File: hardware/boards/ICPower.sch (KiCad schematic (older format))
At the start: 35 parts, among them U1 ECP5UM5G-381caBGA, U3 CYUSB3014, U4 IS43TR16256B-125KBL, U5 128MiB

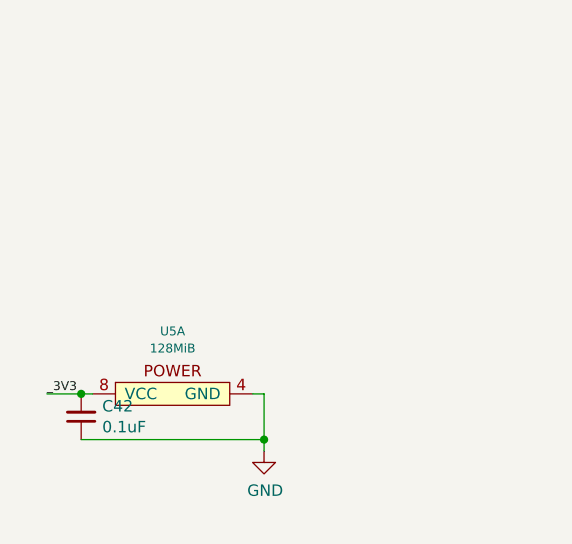
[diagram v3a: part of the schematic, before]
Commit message: Added a secondary SPI flash for the USB PHY Firmware. Yes it's overkill but it'll be fine. I'll use it to like, store configuration data or something
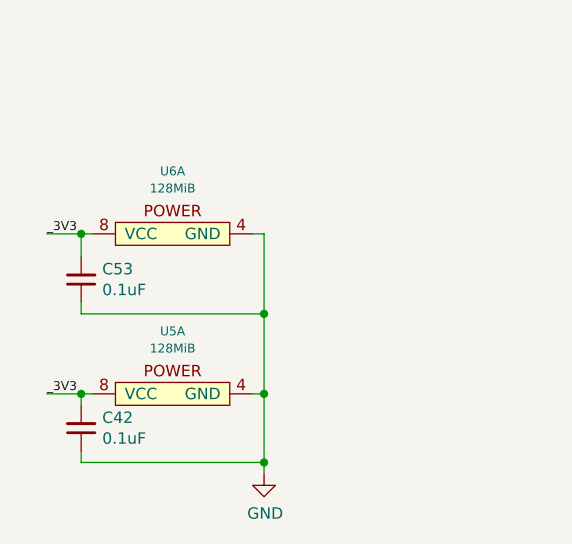
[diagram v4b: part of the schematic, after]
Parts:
- added C53: 0.1uF, Capacitor_SMD:C_0603_1608Metric, symbol Device:C_Small
- added U6: 128MiB, lethalbit-memory:WSON-8-1EP-6.0x8.0mm, symbol lethalbit-memory:W25N01GVZEIG
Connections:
- net 3V3: now also C53.2, U6.8 (VCC)
- net GND: now also C53.1, U6.4 (GND), U6.9 (GND)
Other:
- moved on the sheet: C42
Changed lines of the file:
@@
 	1    0    0    -1
 $EndComp
-Wire Wire Line
-	850  10250 700  10250
 Text Label 700  10250 0    39   ~ 0
 _3V3
@@
 L power:GND #PWR0122
 U 1 1 5F6C47FF
-P 1650 10500
-F 0 "#PWR0122" H 1650 10250 50  0001 C CNN
-F 1 "GND" H 1655 10327 50  0000 C CNN
-F 2 "" H 1650 10500 50  0001 C CNN
-F 3 "" H 1650 10500 50  0001 C CNN
-	1    1650 10500
+P 1650 10600
+F 0 "#PWR0122" H 1650 10350 50  0001 C CNN
+F 1 "GND" H 1655 10427 50  0000 C CNN
+F 2 "" H 1650 10600 50  0001 C CNN
+F 3 "" H 1650 10600 50  0001 C CNN
+	1    1650 10600
 	1    0    0    -1
 $EndComp
 Wire Wire Line
 	1600 10250 1650 10250
-Wire Wire Line
-	1650 10250 1650 10450
 $Comp
 L Device:C_Small C?
 U 1 1 5F7157B7
-P 850 10350
+P 850 10400
 AR Path="/5EDF9F51/5F7157B7" Ref="C?"  Part="1"
 AR Path="/5EF66188/5F7157B7" Ref="C42"  Part="1"
-F 0 "C42" H 758 10304 50  0000 R CNN
-F 1 "0.1uF" H 758 10395 50  0000 R CNN
-F 2 "Capacitor_SMD:C_0603_1608Metric" H 850 10350 50  0001 C CNN
-F 3 "~" H 850 10350 50  0001 C CNN
-F 4 "KEMET" V 850 10350 50  0001 C CNN "MFR"
-F 5 "C0603C104M5RACTU" V 850 10350 50  0001 C CNN "MPN"
-	1    850  10350
+F 0 "C42" H 758 10354 50  0000 R CNN
+F 1 "0.1uF" H 758 10445 50  0000 R CNN
+F 2 "Capacitor_SMD:C_0603_1608Metric" H 850 10400 50  0001 C CNN
+F 3 "~" H 850 10400 50  0001 C CNN
+F 4 "KEMET" V 850 10400 50  0001 C CNN "MFR"
+F 5 "C0603C104M5RACTU" V 850 10400 50  0001 C CNN "MPN"
+	1    850  10400
 	-1   0    0    1
 $EndComp
-Wire Wire Line
-	850  10250 900  10250
-Connection ~ 850  10250
-Wire Wire Line
-	850  10450 1650 10450
-Connection ~ 1650 10450
-Wire Wire Line
-	1650 10450 1650 10500
 Text HLabel 800  1200 0    39   Input ~ 0
 VBUS
@@
 Connection ~ 9500 8350
 Connection ~ 9600 8450
+$Comp
+L lethalbit-memory:W25N01GVZEIG U6
+U 1 1 5FEF8524
+P 1250 9500
+F 0 "U6" H 1250 9724 39  0000 C CNN
+F 1 "128MiB" H 1250 9649 39  0000 C CNN
+F 2 "lethalbit-memory:WSON-8-1EP-6.0x8.0mm" H 1250 9650 39  0001 C CNN
+F 3 "https://www.winbond.com/resource-files/w25n01gv%20revl%20050918%20unsecured.pdf" H 1250 9650 39  0001 C CNN
+F 4 "Winbond" H 1250 9500 50  0001 C CNN "MFR"
+F 5 "W25N01GVZEIG" H 1250 9500 50  0001 C CNN "MPN"
+	1    1250 9500
+	1    0    0    -1
+$EndComp
+Wire Wire Line
+	700  10250 850  10250
+Wire Wire Line
+	850  10250 850  10300
+Connection ~ 850  10250
+Wire Wire Line
+	850  10250 900  10250
+$Comp
+L Device:C_Small C?
+U 1 1 5FF1F758
+P 850 9750
+AR Path="/5EDF9F51/5FF1F758" Ref="C?"  Part="1"
+AR Path="/5EF66188/5FF1F758" Ref="C53"  Part="1"
+F 0 "C53" H 758 9704 50  0000 R CNN
+F 1 "0.1uF" H 758 9795 50  0000 R CNN
+F 2 "Capacitor_SMD:C_0603_1608Metric" H 850 9750 50  0001 C CNN
+F 3 "~" H 850 9750 50  0001 C CNN
+F 4 "KEMET" V 850 9750 50  0001 C CNN "MFR"
+F 5 "C0603C104M5RACTU" V 850 9750 50  0001 C CNN "MPN"
+	1    850  9750
+	-1   0    0    1
+$EndComp
+Wire Wire Line
+	1600 9550 1650 9550
+Wire Wire Line
+	1650 9550 1650 9900
+Connection ~ 1650 10250
+Wire Wire Line
+	900  9550 850  9550
+Wire Wire Line
+	850  9650 850  9550
+Connection ~ 850  9550
+Wire Wire Line
+	850  9550 700  9550
+Wire Wire Line
+	850  9850 850  9900
+Wire Wire Line
+	850  9900 1650 9900
+Connection ~ 1650 9900
+Wire Wire Line
+	1650 9900 1650 10250
+Wire Wire Line
+	1650 10250 1650 10550
+Wire Wire Line
+	850  10500 850  10550
+Wire Wire Line
+	850  10550 1650 10550
+Connection ~ 1650 10550
+Wire Wire Line
+	1650 10550 1650 10600
+Text Label 700  9550 0    39   ~ 0
+_3V3
 $EndSCHEMATC

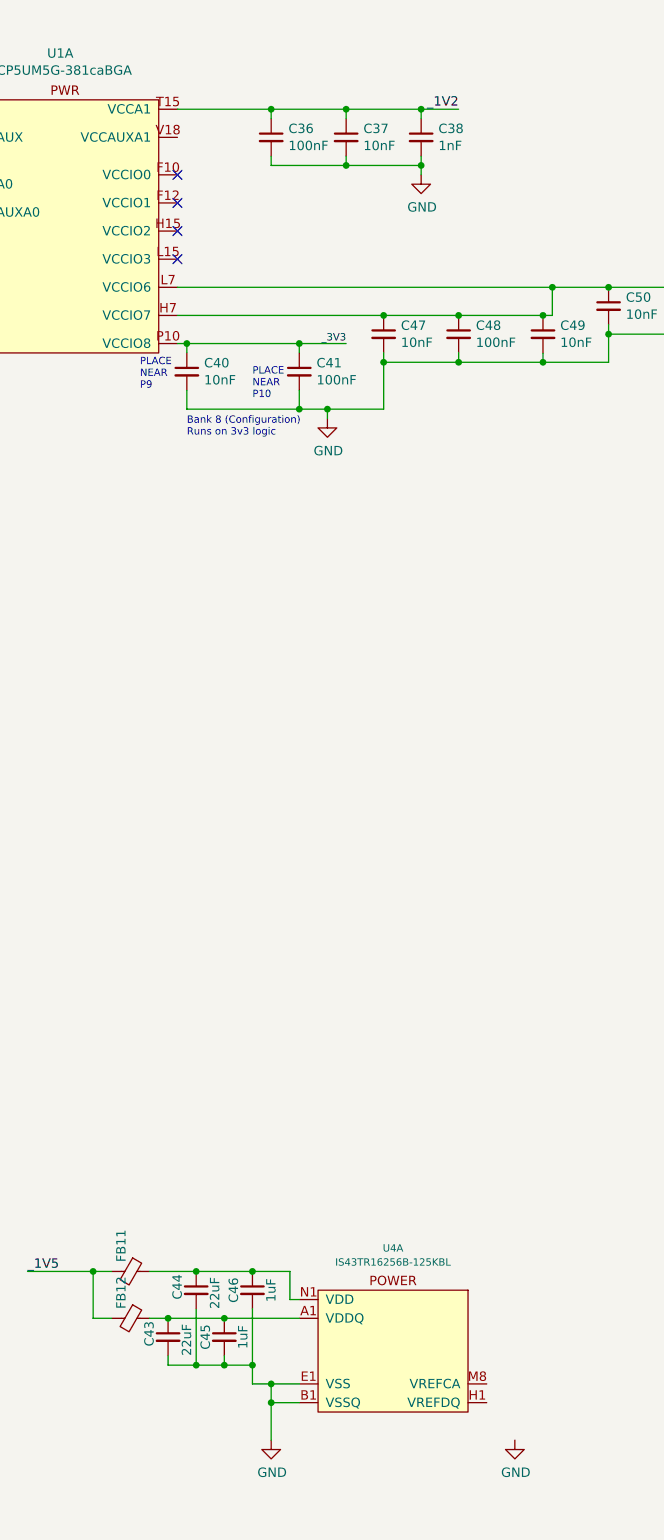
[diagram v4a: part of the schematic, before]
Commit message: Some ERC cleanup
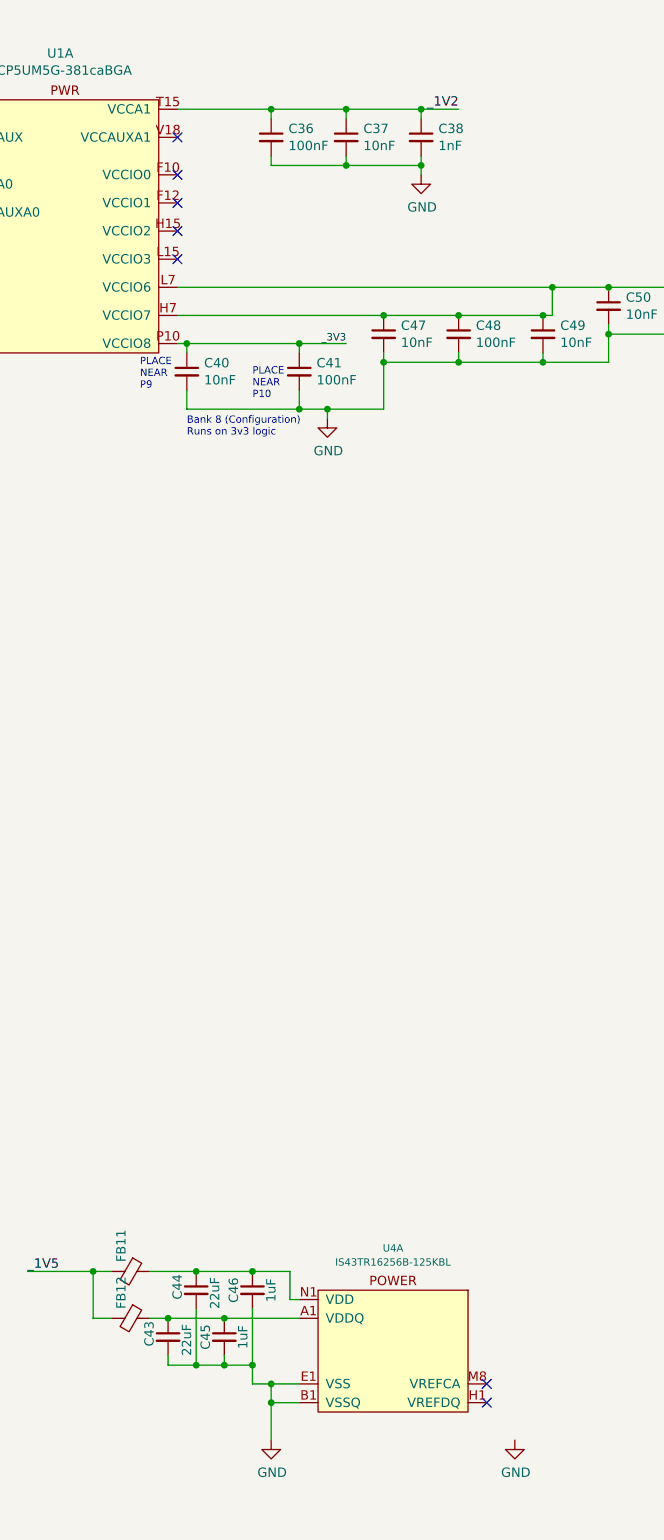
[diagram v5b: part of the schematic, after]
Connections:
- no-connect marks 17 -> 20
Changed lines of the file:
@@
 Text Label 700  9550 0    39   ~ 0
 _3V3
+NoConn ~ 9100 1800
+NoConn ~ 10750 8450
+NoConn ~ 10750 8550
 $EndSCHEMATC

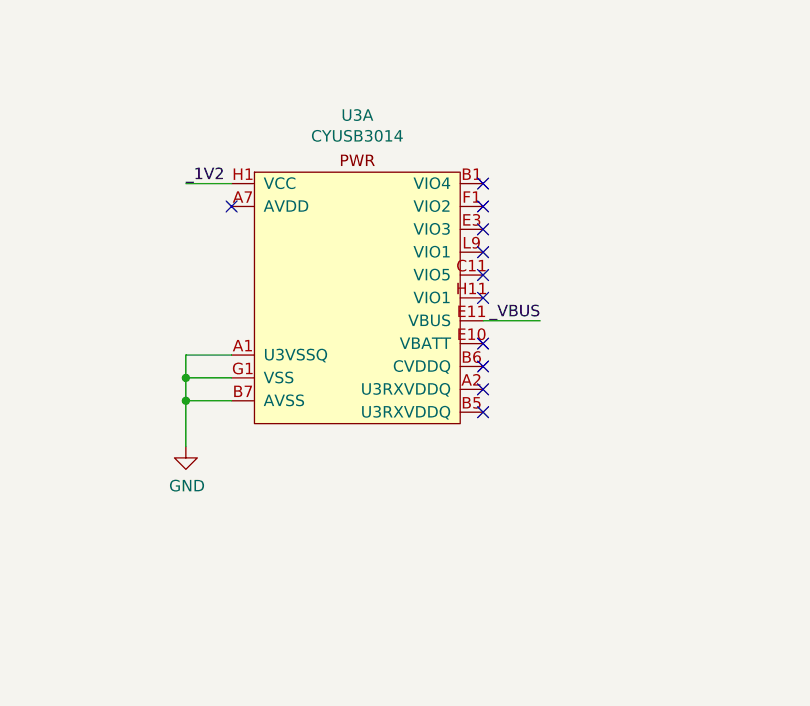
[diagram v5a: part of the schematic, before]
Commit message: Added the power hookups for the USB PHY
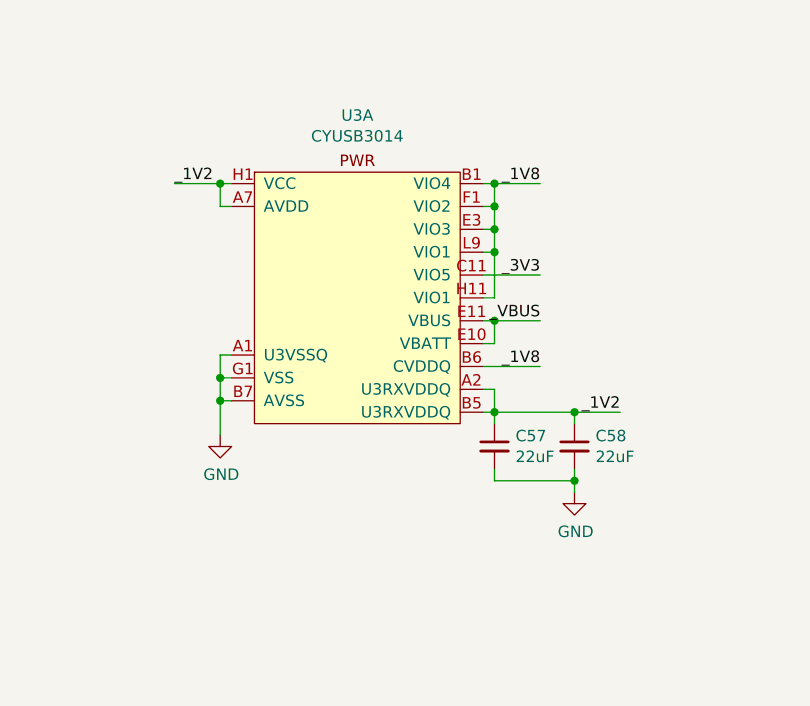
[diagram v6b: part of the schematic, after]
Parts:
- added C57, C58: 22uF, Capacitor_SMD:C_0805_2012Metric, symbol Device:C_Small
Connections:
- net 1V2: now also U3.A2 (U3RXVDDQ), U3.A7 (AVDD), U3.B5 (U3RXVDDQ), C57.1, C58.1
- net 1V8: now also U3.B1 (VIO4), U3.B6 (CVDDQ), U3.E3 (VIO3), U3.F1 (VIO2), U3.H11 (VIO1), U3.L9 (VIO1)
- net 3V3: now also U3.C11 (VIO5)
- net GND: now also C57.2, C58.2
- net VBUS: now also U3.E10 (VBATT)
- no-connect marks 20 -> 9
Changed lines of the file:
@@
 L power:GND #PWR0113
 U 1 1 5F6ECAA7
-P 5000 5850
-F 0 "#PWR0113" H 5000 5600 50  0001 C CNN
-F 1 "GND" H 5005 5677 50  0000 C CNN
-F 2 "" H 5000 5850 50  0001 C CNN
-F 3 "" H 5000 5850 50  0001 C CNN
-	1    5000 5850
+P 5150 5800
+F 0 "#PWR0113" H 5150 5550 50  0001 C CNN
+F 1 "GND" H 5155 5627 50  0000 C CNN
+F 2 "" H 5150 5800 50  0001 C CNN
+F 3 "" H 5150 5800 50  0001 C CNN
+	1    5150 5800
 	1    0    0    -1
 $EndComp
@@
 	7750 2900 7750 3000
 Wire Wire Line
-	5200 5450 5000 5450
-Wire Wire Line
-	5000 5450 5000 5550
-Wire Wire Line
-	5200 5550 5000 5550
-Connection ~ 5000 5550
-Wire Wire Line
-	5000 5550 5000 5650
-Wire Wire Line
-	5200 5650 5000 5650
-Connection ~ 5000 5650
-Wire Wire Line
-	5000 5650 5000 5850
+	5200 5450 5150 5450
+Wire Wire Line
+	5150 5450 5150 5550
+Wire Wire Line
+	5200 5550 5150 5550
+Connection ~ 5150 5550
+Wire Wire Line
+	5150 5550 5150 5650
+Wire Wire Line
+	5200 5650 5150 5650
+Connection ~ 5150 5650
+Wire Wire Line
+	5150 5650 5150 5800
 $Comp
 L power:GND #PWR0115
@@
 	800  1100 1950 1100
 Wire Wire Line
-	5200 4700 5000 4700
-Text Label 5000 4700 0    50   ~ 0
+	5200 4700 5150 4700
+Text Label 4950 4700 0    50   ~ 0
 _1V2
 Wire Wire Line
@@
 Wire Wire Line
 	9100 1650 9600 1650
-NoConn ~ 5200 4800
-NoConn ~ 6300 4700
-NoConn ~ 6300 4800
-NoConn ~ 6300 4900
-NoConn ~ 6300 5000
-NoConn ~ 6300 5100
-NoConn ~ 6300 5200
-NoConn ~ 6300 5400
-NoConn ~ 6300 5500
-NoConn ~ 6300 5600
-NoConn ~ 6300 5700
 NoConn ~ 7850 2200
 NoConn ~ 7850 1800
@@
 _VBUS
 Wire Wire Line
-	6300 5300 6550 5300
+	6300 5300 6350 5300
 Text Label 6550 5300 2    50   ~ 0
 _VBUS
@@
 NoConn ~ 10750 8450
 NoConn ~ 10750 8550
+Wire Wire Line
+	5200 4800 5150 4800
+Wire Wire Line
+	5150 4800 5150 4700
+Connection ~ 5150 4700
+Wire Wire Line
+	5150 4700 4950 4700
+$Comp
+L Device:C_Small C?
+U 1 1 608EC3F2
+P 6350 5850
+AR Path="/5EDF9F51/608EC3F2" Ref="C?"  Part="1"
+AR Path="/5EF66188/608EC3F2" Ref="C57"  Part="1"
+F 0 "C57" H 6442 5896 50  0000 L CNN
+F 1 "22uF" H 6442 5805 50  0000 L CNN
+F 2 "Capacitor_SMD:C_0805_2012Metric" H 6350 5850 50  0001 C CNN
+F 3 "~" H 6350 5850 50  0001 C CNN
+F 4 "KEMET" H 6350 5850 50  0001 C CNN "MFR"
+F 5 "C0805C226M9PACTU" H 6350 5850 50  0001 C CNN "MPN"
+	1    6350 5850
+	1    0    0    -1
+$EndComp
+$Comp
+L Device:C_Small C?
+U 1 1 608F2F1F
+P 6700 5850
+AR Path="/5EDF9F51/608F2F1F" Ref="C?"  Part="1"
+AR Path="/5EF66188/608F2F1F" Ref="C58"  Part="1"
+F 0 "C58" H 6792 5896 50  0000 L CNN
+F 1 "22uF" H 6792 5805 50  0000 L CNN
+F 2 "Capacitor_SMD:C_0805_2012Metric" H 6700 5850 50  0001 C CNN
+F 3 "~" H 6700 5850 50  0001 C CNN
+F 4 "KEMET" H 6700 5850 50  0001 C CNN "MFR"
+F 5 "C0805C226M9PACTU" H 6700 5850 50  0001 C CNN "MPN"
+	1    6700 5850
+	1    0    0    -1
+$EndComp
+Wire Wire Line
+	6300 5600 6350 5600
+Wire Wire Line
+	6300 5700 6350 5700
+Wire Wire Line
+	6350 5700 6350 5750
+$Comp
+L power:GND #PWR0131
+U 1 1 6090388C
+P 6700 6050
+F 0 "#PWR0131" H 6700 5800 50  0001 C CNN
+F 1 "GND" H 6705 5877 50  0000 C CNN
+F 2 "" H 6700 6050 50  0001 C CNN
+F 3 "" H 6700 6050 50  0001 C CNN
+	1    6700 6050
+	1    0    0    -1
+$EndComp
+Wire Wire Line
+	6350 5950 6350 6000
+Wire Wire Line
+	6350 6000 6700 6000
+Wire Wire Line
+	6700 6000 6700 6050
+Wire Wire Line
+	6700 5950 6700 6000
+Connection ~ 6700 6000
+Wire Wire Line
+	6350 5700 6700 5700
+Connection ~ 6350 5700
+Wire Wire Line
+	6700 5700 6700 5750
+Wire Wire Line
+	6350 5600 6350 5700
+Wire Wire Line
+	6700 5700 6900 5700
+Connection ~ 6700 5700
+Text Label 6900 5700 2    50   ~ 0
+_1V2
+Wire Wire Line
+	6300 5500 6550 5500
+Text Label 6550 5500 2    50   ~ 0
+_1V8
+Wire Wire Line
+	6300 4700 6350 4700
+Wire Wire Line
+	6300 4800 6350 4800
+Wire Wire Line
+	6350 4800 6350 4700
+Connection ~ 6350 4700
+Wire Wire Line
+	6350 4700 6550 4700
+Wire Wire Line
+	6300 4900 6350 4900
+Wire Wire Line
+	6350 4900 6350 4800
+Connection ~ 6350 4800
+Wire Wire Line
+	6300 5000 6350 5000
+Wire Wire Line
+	6350 5000 6350 4900
+Connection ~ 6350 4900
+Text Label 6550 4700 2    50   ~ 0
+_1V8
+Wire Wire Line
+	6350 5300 6350 5400
+Wire Wire Line
+	6350 5400 6300 5400
+Connection ~ 6350 5300
+Wire Wire Line
+	6350 5300 6550 5300
+Wire Wire Line
+	6300 5100 6550 5100
+Text Label 6550 5100 2    50   ~ 0
+_3V3
+Wire Wire Line
+	6300 5200 6350 5200
+Wire Wire Line
+	6350 5200 6350 5000
+Connection ~ 6350 5000
 $EndSCHEMATC

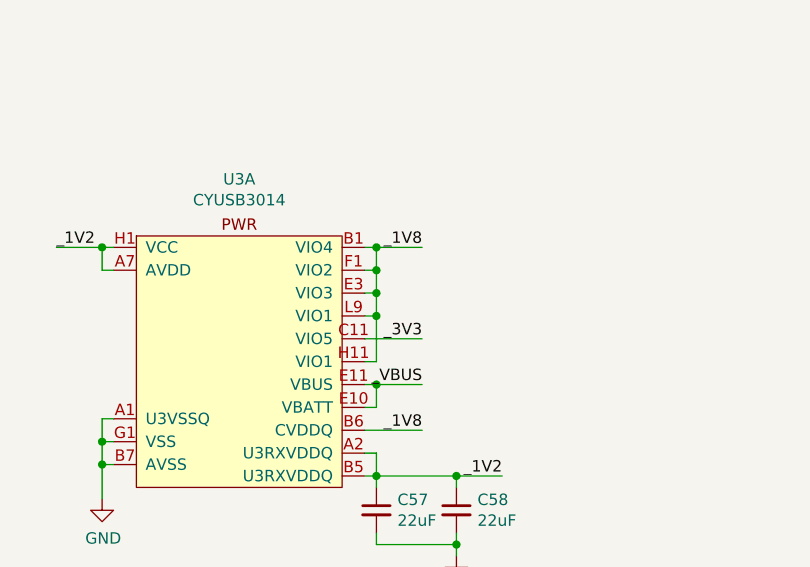
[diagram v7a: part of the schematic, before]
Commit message: Fixed the VIO4 rail of the USB PHY to be 3v3 not 1v8
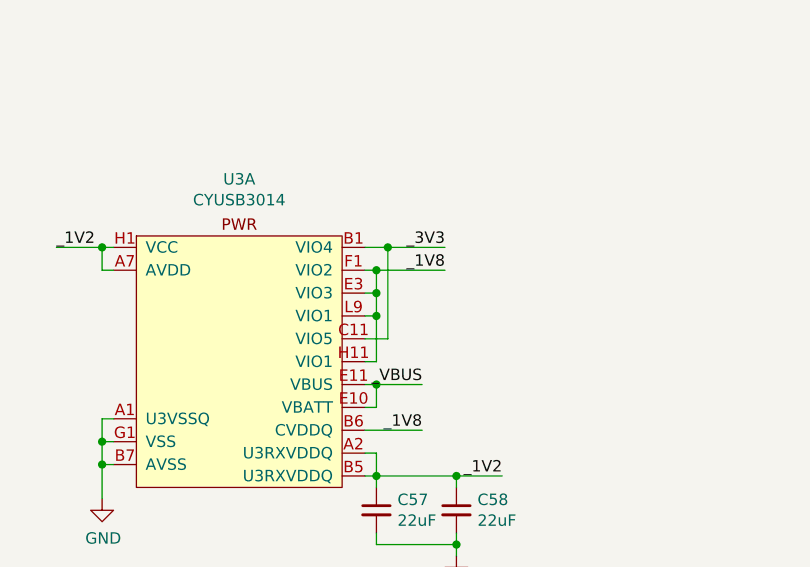
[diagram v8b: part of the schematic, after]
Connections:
- net 1V8: no longer U3.B1 (VIO4)
- net 3V3: now also U3.B1 (VIO4)
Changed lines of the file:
@@
 _1V8
 Wire Wire Line
-	6300 4700 6350 4700
-Wire Wire Line
 	6300 4800 6350 4800
-Wire Wire Line
-	6350 4800 6350 4700
-Connection ~ 6350 4700
-Wire Wire Line
-	6350 4700 6550 4700
 Wire Wire Line
 	6300 4900 6350 4900
 Wire Wire Line
 	6350 4900 6350 4800
-Connection ~ 6350 4800
 Wire Wire Line
 	6300 5000 6350 5000
@@
 	6350 5000 6350 4900
 Connection ~ 6350 4900
-Text Label 6550 4700 2    50   ~ 0
+Text Label 6650 4800 2    50   ~ 0
 _1V8
 Wire Wire Line
@@
 	6350 5300 6550 5300
 Wire Wire Line
-	6300 5100 6550 5100
-Text Label 6550 5100 2    50   ~ 0
+	6300 5100 6400 5100
+Text Label 6650 4700 2    50   ~ 0
 _3V3
 Wire Wire Line
@@
 	6350 5200 6350 5000
 Connection ~ 6350 5000
+Wire Wire Line
+	6300 4700 6400 4700
+Wire Wire Line
+	6350 4800 6650 4800
+Connection ~ 6350 4800
+Wire Wire Line
+	6400 5100 6400 4700
+Connection ~ 6400 4700
+Wire Wire Line
+	6400 4700 6650 4700
 $EndSCHEMATC
